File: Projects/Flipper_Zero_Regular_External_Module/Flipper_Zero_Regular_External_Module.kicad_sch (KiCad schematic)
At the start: 1 part, among them J1 Flipper_Zero

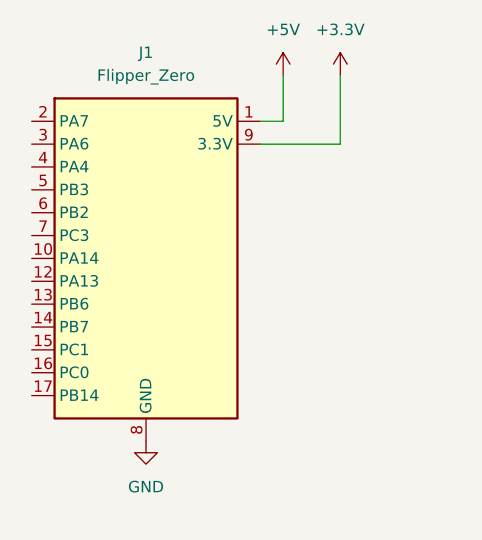
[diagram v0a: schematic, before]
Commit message: Update to KiCAD 10
Signed-off-by: Ilias Daradimos <judgedrid@gmail.com>
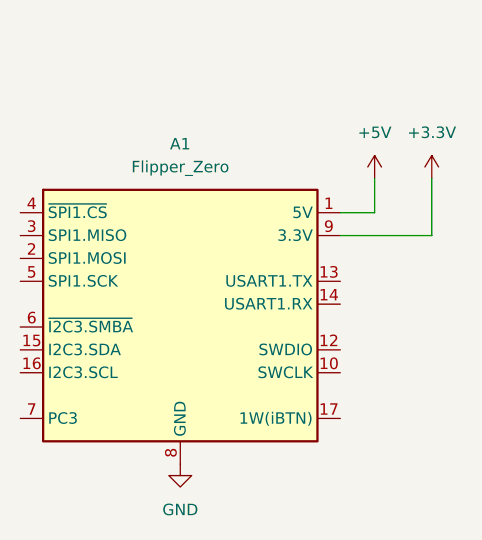
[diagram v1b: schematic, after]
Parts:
- removed J1: Flipper_Zero, Module:Flipper_Zero_Angled, symbol MCU_Module:Flipper_Zero
- added A1: Flipper_Zero, Module:Flipper_Zero_Angled, symbol MCU_Module:Flipper_Zero
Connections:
- net +3.3V: now also A1.9 (3.3V)
- net +5V: now also A1.1 (5V)
- net GND: now also A1.11 (GND), A1.18 (GND), A1.8 (GND)
